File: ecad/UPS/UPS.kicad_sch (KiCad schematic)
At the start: 0 parts

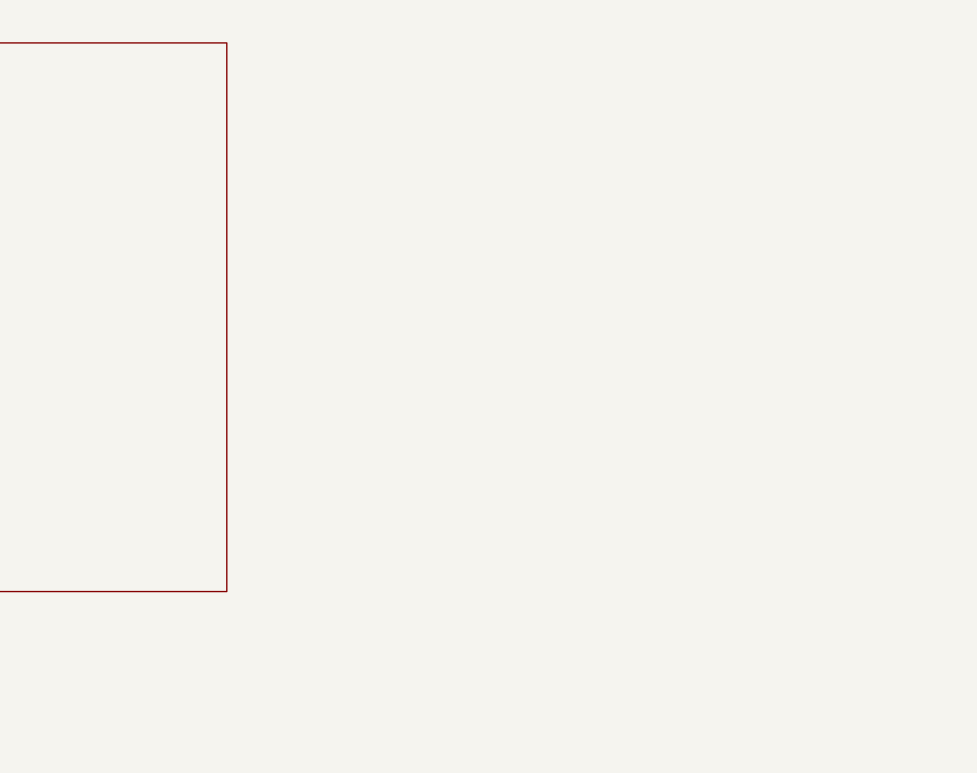
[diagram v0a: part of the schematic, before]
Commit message: Made Buck Convertor Schematic
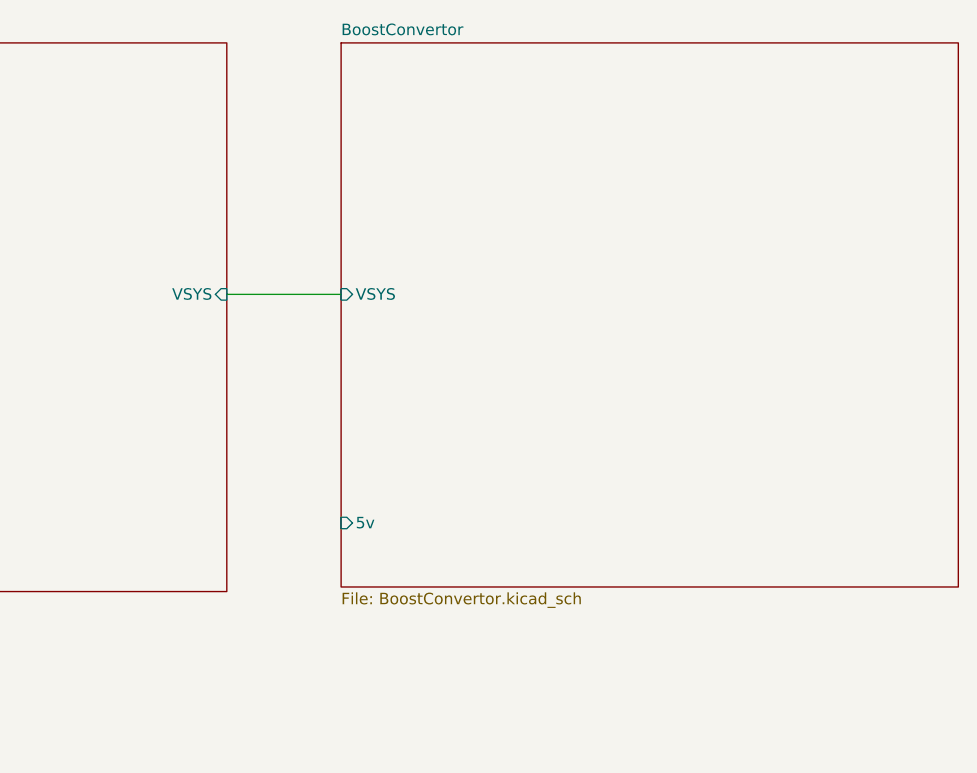
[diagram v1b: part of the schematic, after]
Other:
- added sheet BoostConvertor (BoostConvertor.kicad_sch)
- sheet Charger ports: added VSYS; removed none
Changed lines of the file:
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@@
 	(generator_version "9.0")
 	(paper "A4")
+	(wire
+		(pts
+			(xy 100.33 55.88) (xy 113.03 55.88)
+		)
+		(stroke
+			(width 0)
+			(type default)
+		)
+	)
 	(sheet
 		(at 26.67 27.94)
@@
 			)
 		)
+		(pin "VSYS" input
+			(at 100.33 55.88 0)
+			(effects
+				(font
+					(size 1.27 1.27)
+				)
+				(justify right)
+			)
+		)
 		(instances
 			(project "UPS"
@@
 				)
 			)
+		)
+	)
+	(sheet
+		(at 113.03 27.94)
+		(size 68.58 60.452)
+		(exclude_from_sim no)
+		(in_bom yes)
+		(on_board yes)
+		(dnp no)
+		(fields_autoplaced yes)
+		(stroke
+			(width 0.1524)
+			(type solid)
+		)
+		(fill
+			(color 0 0 0 0.0000)
+		)
+		(property "Sheetname" "BoostConvertor"
+			(at 113.03 27.2284 0)
+			(effects
+				(font
+					(size 1.27 1.27)
+				)
+				(justify left bottom)
+			)
+		)
+		(property "Sheetfile" "BoostConvertor.kicad_sch"
+			(at 113.03 88.9766 0)
+			(effects
+				(font
+					(size 1.27 1.27)
+				)
+				(justify left top)
+			)
+		)
+		(pin "VSYS" input
+			(at 113.03 55.88 180)
+			(effects
+				(font
+					(size 1.27 1.27)
+				)
+				(justify left)
+			)
+		)
+		(pin "5v" input
+			(at 113.03 81.28 180)
+			(effects
+				(font
+					(size 1.27 1.27)
+				)
+				(justify left)
+			)
+		)
+		(instances
+			(project "UPS"
+				(path "/9d92b60a-4a6b-449c-b462-cab19e69d38c"
+					(page "4")
+				)
+			)

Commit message: Misc repo cleanup
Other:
- sheet Charger: file untitled.kicad_sch -> Charger.kicad_sch
- company: (none) -> MTU Open Source Hardware Enterprise
- title: (none) -> UPS
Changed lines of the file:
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@@
 	(generator_version "9.0")
 	(paper "A4")
+	(title_block
+		(title "UPS")
+		(company "MTU Open Source Hardware Enterprise")
+	)
 	(wire
 		(pts
@@
 			)
 		)
-		(property "Sheetfile" "untitled.kicad_sch"
+		(property "Sheetfile" "Charger.kicad_sch"
 			(at 26.67 89.4846 0)
 			(effects

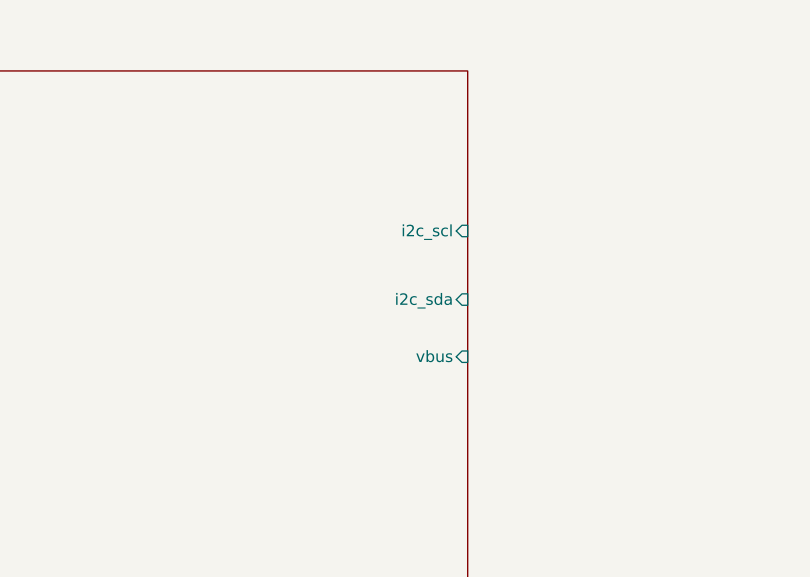
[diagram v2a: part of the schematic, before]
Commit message: Handle PD GPIO pins
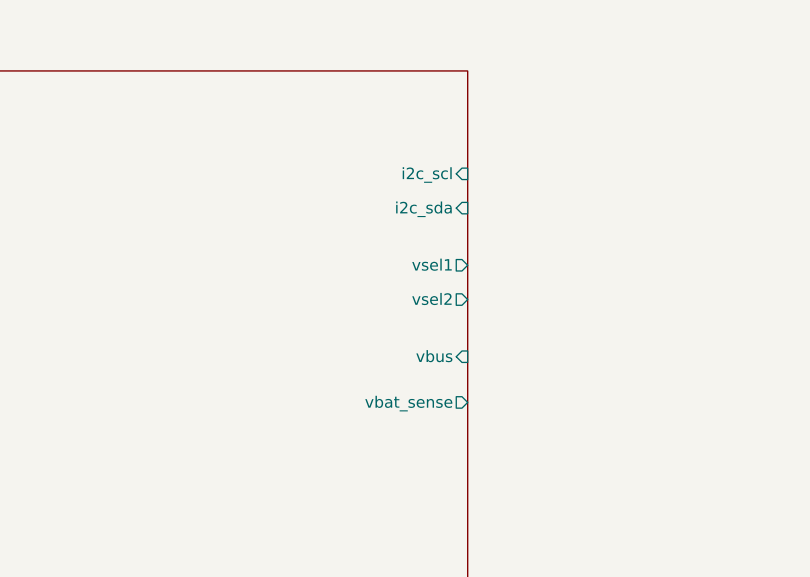
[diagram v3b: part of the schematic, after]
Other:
- sheet Output ports: added vbat_sense, vsel1, vsel2; removed none
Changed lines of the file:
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@@
 		)
 		(pin "i2c_scl" input
-			(at 104.14 139.7 0)
+			(at 104.14 133.35 0)
 			(effects
 				(font
@@
 		)
 		(pin "i2c_sda" input
-			(at 104.14 147.32 0)
+			(at 104.14 137.16 0)
 			(effects
 				(font
@@
 			(effects
 				(font
+					(size 1.27 1.27)
+				)
+				(justify right)
+			)
+		)
+		(pin "vbat_sense" output
+			(at 104.14 158.75 0)
+			(effects
+				(font
+					(size 1.27 1.27)
+				)
+				(justify right)
+			)
+		)
+		(pin "vsel1" output
+			(at 104.14 143.51 0)
+			(effects
+				(font
+					(size 1.27 1.27)
+				)
+				(justify right)
+			)
+		)
+		(pin "vsel2" output
+			(at 104.14 147.32 0)
+			(effects
+				(font
